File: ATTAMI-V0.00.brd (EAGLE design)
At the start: 22.8 x 22.9 mm, 26 parts, among them U1 MIC5225, U2 ATTINY85-20SU

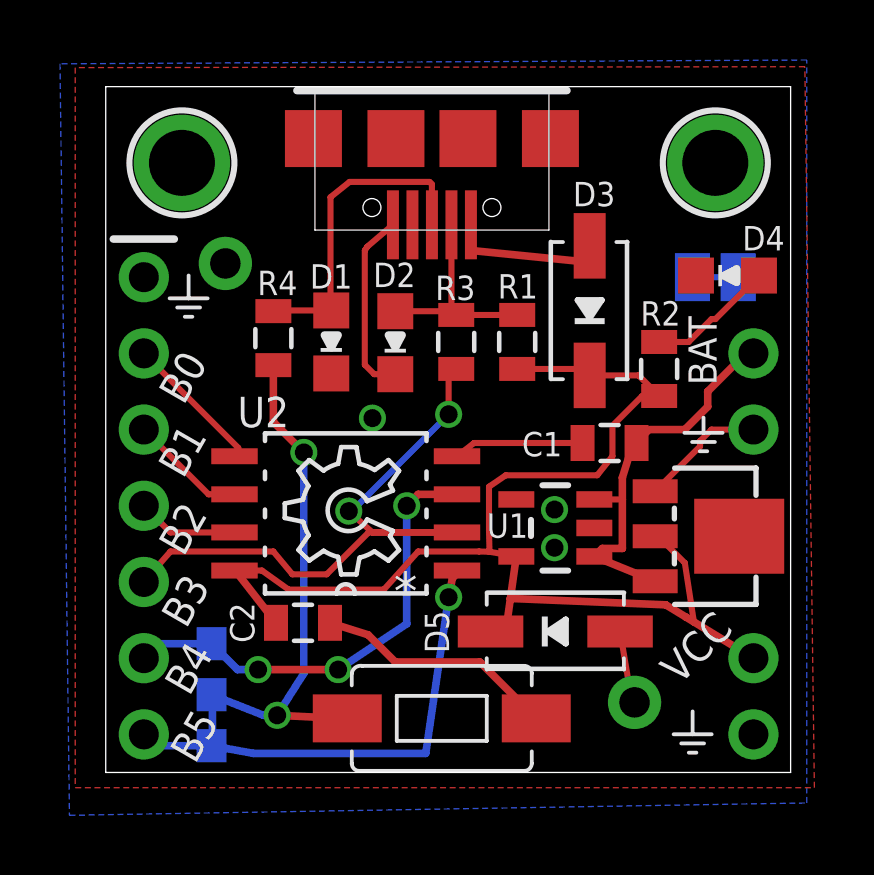
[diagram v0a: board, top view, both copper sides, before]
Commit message: pushed the pb5 wire a bit to the cneter
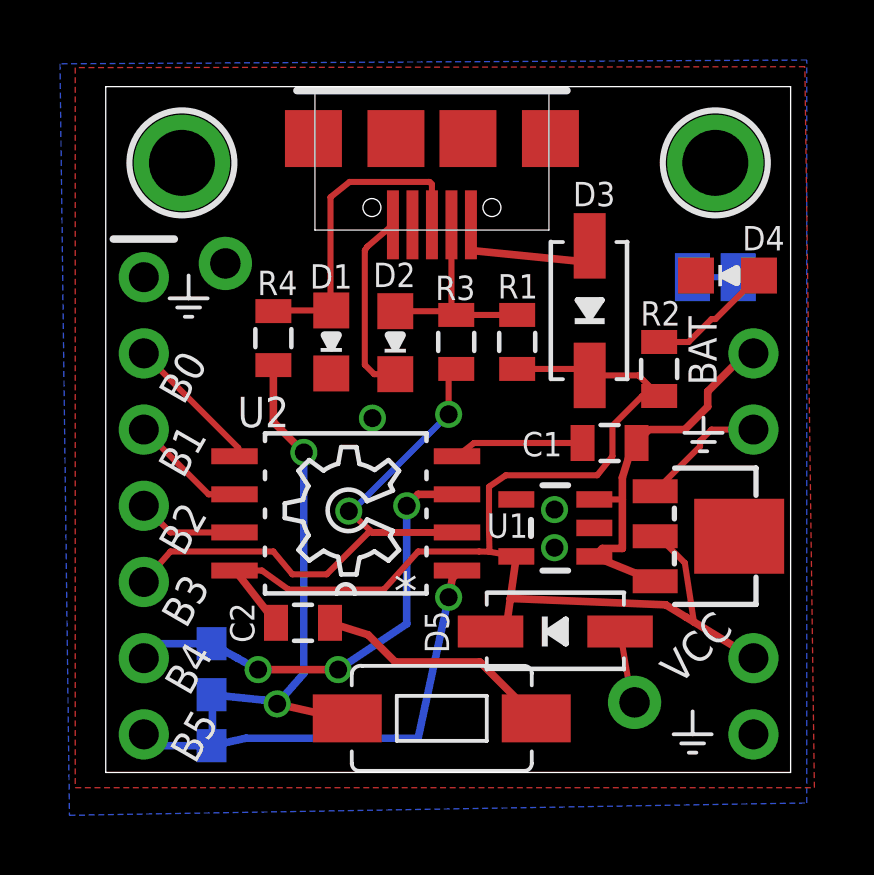
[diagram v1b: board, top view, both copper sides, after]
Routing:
- net PB5: track 15.8 -> 15.1 mm
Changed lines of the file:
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@@
 <wire x1="7.747" y1="3.429" x2="5.08" y2="3.429" width="0.254" layer="1"/>
 <via x="5.08" y="3.429" extent="1-16" drill="0.6"/>
-<wire x1="5.08" y1="3.429" x2="4.3924" y2="3.429" width="0.254" layer="16"/>
-<wire x1="4.3924" y1="3.429" x2="3.5306" y2="4.2908" width="0.254" layer="16"/>
+<wire x1="5.08" y1="3.429" x2="4.3924" y2="3.81" width="0.254" layer="16"/>
+<wire x1="4.3924" y1="3.81" x2="3.5306" y2="4.2908" width="0.254" layer="16"/>
 </signal>
 <signal name="PB5">
@@
 <wire x1="1.6492" y1="0.8908" x2="1.27" y2="1.27" width="0.254" layer="16"/>
 <via x="11.43" y="5.842" extent="1-16" drill="0.6"/>
-<wire x1="11.43" y1="5.842" x2="10.668" y2="0.635" width="0.254" layer="16"/>
-<wire x1="10.668" y1="0.635" x2="4.9294" y2="0.635" width="0.254" layer="16"/>
-<wire x1="4.9294" y1="0.635" x2="3.5306" y2="0.8908" width="0.254" layer="16"/>
+<wire x1="11.43" y1="5.842" x2="10.414" y2="1.143" width="0.254" layer="16"/>
+<wire x1="10.414" y1="1.143" x2="4.6754" y2="1.143" width="0.254" layer="16"/>
+<wire x1="4.6754" y1="1.143" x2="3.5306" y2="0.8908" width="0.254" layer="16"/>
 </signal>
 <signal name="V_BAT">
@@
 <contactref element="S1" pad="P$2"/>
 <wire x1="8.0514" y1="1.8034" x2="7.8486" y2="1.8034" width="0.254" layer="1"/>
-<wire x1="7.8486" y1="1.8034" x2="5.715" y2="1.905" width="0.254" layer="1"/>
-<via x="5.715" y="1.905" extent="1-16" drill="0.6"/>
-<wire x1="5.715" y1="1.905" x2="5.2578" y2="1.905" width="0.254" layer="16"/>
-<wire x1="5.2578" y1="1.905" x2="3.5306" y2="2.5908" width="0.254" layer="16"/>
+<wire x1="7.8486" y1="1.8034" x2="5.715" y2="2.286" width="0.254" layer="1"/>
+<via x="5.715" y="2.286" extent="1-16" drill="0.6"/>
+<wire x1="5.715" y1="2.286" x2="5.2578" y2="2.413" width="0.254" layer="16"/>
+<wire x1="5.2578" y1="2.413" x2="3.5306" y2="2.5908" width="0.254" layer="16"/>
 <wire x1="5.588" y1="13.578" x2="5.588" y2="11.684" width="0.254" layer="1"/>
 <wire x1="5.588" y1="11.684" x2="6.604" y2="10.668" width="0.254" layer="1"/>
 <via x="6.604" y="10.668" extent="1-16" drill="0.6"/>
 <wire x1="6.604" y1="10.668" x2="6.604" y2="3.302" width="0.254" layer="16"/>
-<wire x1="6.604" y1="3.302" x2="5.715" y2="1.905" width="0.254" layer="16"/>
+<wire x1="6.604" y1="3.302" x2="5.715" y2="2.286" width="0.254" layer="16"/>
 </signal>
 <signal name="N$3">

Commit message: hl version
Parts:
- SJ1: value (none) -> JUMPER-PAD-2-NC_BY_TRACE; device ATtami:SOLDERJUMPER_CLOSEDWIRE -> SparkFun-Passives:PAD-JUMPER-2-NC_BY_TRACE_YES_SILK
- SJ2: value (none) -> JUMPER-PAD-3-2OF3_NC_BY_TRACE_SMALL; device microbuilder:SOLDERJUMPER_2WAY_OPEN_0603 -> SparkFun-Passives:PAD-JUMPER-3-2OF3_NC_BY_TRACE_YES_SILK_FULL_BOX
- moved R2 0.28 mm to (18.7, 13.6)
- moved SJ1 0.23 mm to (20.5, 16.5)
- moved SJ2 0.22 mm to (3.45, 2.39)
- moved D3 0.18 mm to (16.3, 15.5)
- moved D4 0.18 mm to (20.6, 16.6), turned to 270 degrees
- moved D2 0.15 mm to (9.53, 14.2), turned to 0 degrees
- moved D1 0.05 mm to (7.47, 14.4), turned to 0 degrees
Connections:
- net GND: now also 1117.GND, S1.P$2, USB.GND; no longer 1117.1, S1.P$1, USB.GND@1
- net N$1: no longer S1.P$2
- net PB5: now also S1.P$1
- net VCC: now also 1117.VOUT@1, 1117.VOUT@2; no longer 1117.2
- net V_BAT: now also 1117.VIN; no longer 1117.3
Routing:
- net GND: track 23.3 -> 10.0 mm, vias 3 -> 2
- net VCC: track 42.2 -> 48.1 mm
- net PB5: track 15.1 -> 20.7 mm, vias 1 -> 2
- net N$7: track 11.6 -> 7.42 mm
- net N$13: track 0.00 -> 3.94 mm, vias 0 -> 1
- net PB4: track 15.4 -> 17.8 mm, vias 3 -> 2
- net N$1: track 16.6 -> 14.5 mm, vias 2 -> 1
- net N$3: track 1.40 -> 0.00 mm
- net PB3: track 22.0 -> 21.2 mm
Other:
- board text added: "4"
- board text added: "5"
- board text removed: "PB4"
- board text removed: "PB5"

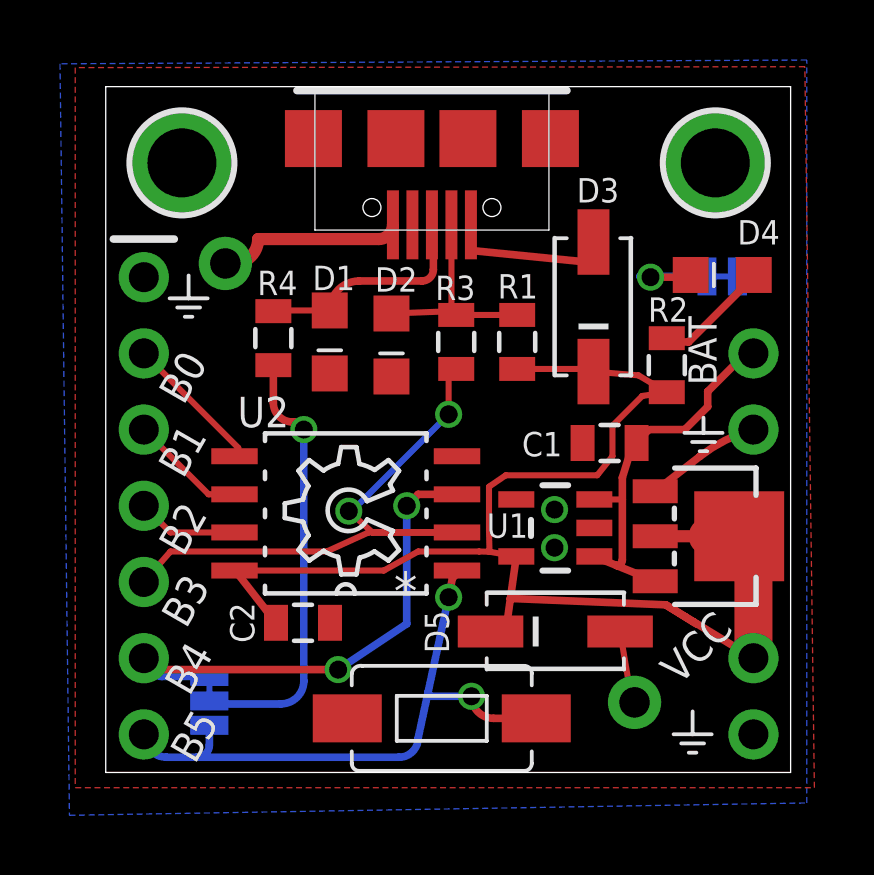
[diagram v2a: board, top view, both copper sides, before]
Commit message: Some changes of the routing
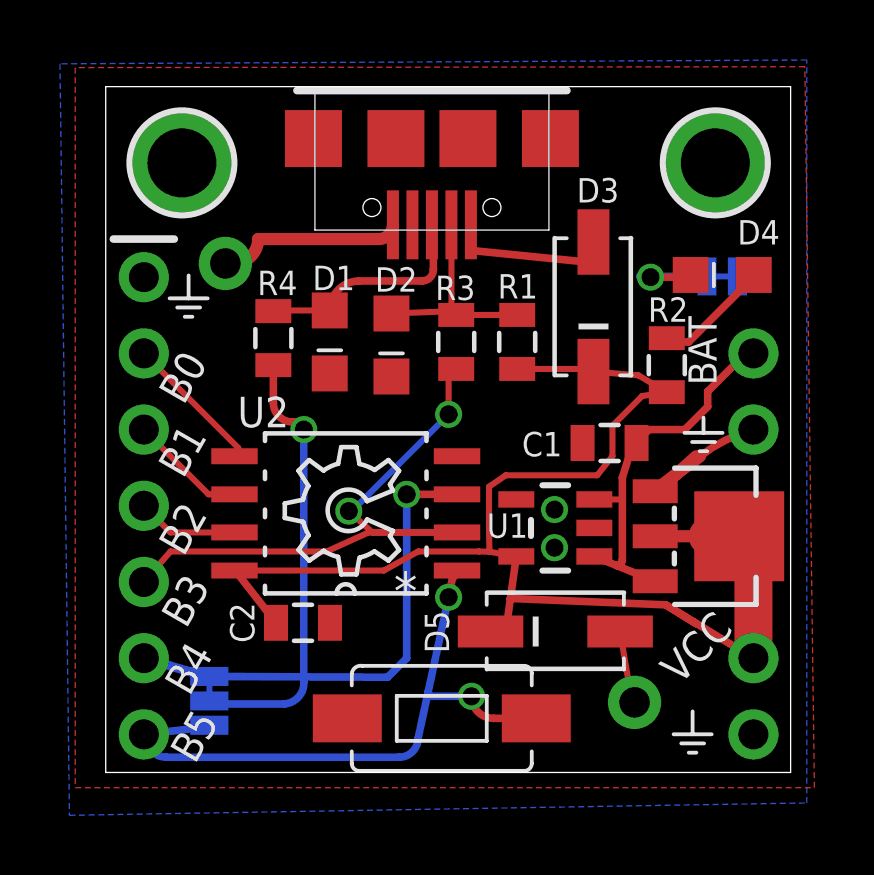
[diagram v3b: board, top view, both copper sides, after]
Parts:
- U3: value (none) -> 1117
- renumbered 1117 to U3
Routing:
- net GND: track 10.0 -> 12.0 mm
- net PB4: track 17.8 -> 16.2 mm, vias 2 -> 1
- net PB5: track 20.7 -> 21.6 mm
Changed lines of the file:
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@@
 <attribute name="NAME" x="4.3942" y="11.5062" size="1.016" layer="25" ratio="10" rot="SR0"/>
 </element>
-<element name="1117" library="ATtami" package="SOT89" value="" x="20.066" y="7.874" smashed="yes" rot="R270">
+<element name="U3" library="ATtami" package="SOT89" value="1117" x="20.066" y="7.874" smashed="yes" rot="R270">
 <attribute name="VALUE" x="16.241" y="10.079" size="1.27" layer="27" rot="R270"/>
 </element>
@@
 <contactref element="COIN_CELL_(-)" pad="1"/>
 <contactref element="U2" pad="4"/>
-<contactref element="1117" pad="GND"/>
 <via x="14.9606" y="8.763" extent="1-16" drill="0.6"/>
 <via x="14.9606" y="7.493" extent="1-16" drill="0.6"/>
@@
 <wire x1="5.08" y1="17.78" x2="4.2672" y2="16.9672" width="0.4064" layer="1" curve="-90"/>
 <wire x1="4.2672" y1="16.9672" x2="3.9878" y2="16.9672" width="0.4064" layer="1"/>
-<wire x1="18.316" y1="9.374" x2="19.812" y2="10.541" width="0.254" layer="1"/>
 <wire x1="19.812" y1="10.541" x2="21.59" y2="11.43" width="0.254" layer="1" curve="-22.784078"/>
+<contactref element="U3" pad="GND"/>
+<wire x1="18.288" y1="9.398" x2="19.812" y2="10.541" width="0.4064" layer="1"/>
+<wire x1="18.415" y1="9.398" x2="19.685" y2="10.541" width="0.4064" layer="1"/>
+<wire x1="18.288" y1="9.398" x2="18.415" y2="9.398" width="0.4064" layer="1"/>
+<wire x1="18.542" y1="9.398" x2="18.415" y2="9.398" width="0.4064" layer="1"/>
+<wire x1="18.288" y1="9.398" x2="18.316" y2="9.374" width="0" layer="19" extent="1-1"/>
 </signal>
 <signal name="PB3">
@@
 <contactref element="J1" pad="6"/>
 <contactref element="U2" pad="3"/>
-<wire x1="11.7094" y1="9.271" x2="10.414" y2="9.271" width="0.254" layer="1"/>
-<wire x1="10.414" y1="9.271" x2="10.033" y2="8.89" width="0.254" layer="1"/>
-<via x="10.033" y="8.89" extent="1-16" drill="0.6"/>
-<wire x1="10.033" y1="8.89" x2="10.033" y2="4.953" width="0.254" layer="16"/>
-<wire x1="10.033" y1="4.953" x2="7.747" y2="3.429" width="0.254" layer="16"/>
-<via x="7.747" y="3.429" extent="1-16" drill="0.6"/>
 <contactref element="SJ2" pad="3"/>
-<wire x1="3.4544" y1="3.2004" x2="1.8796" y2="3.2004" width="0.254" layer="16"/>
-<wire x1="1.8796" y1="3.2004" x2="1.27" y2="3.81" width="0.254" layer="16" curve="-90"/>
-<wire x1="7.747" y1="3.429" x2="1.27" y2="3.429" width="0.254" layer="1"/>
-<wire x1="1.27" y1="3.429" x2="1.27" y2="3.81" width="0.254" layer="1"/>
+<wire x1="3.429" y1="3.175" x2="1.27" y2="3.81" width="0.3048" layer="16"/>
+<wire x1="3.4544" y1="3.2004" x2="9.398" y2="3.175" width="0.254" layer="16"/>
+<wire x1="9.398" y1="3.175" x2="10.033" y2="3.81" width="0.254" layer="16"/>
+<wire x1="10.033" y1="3.81" x2="10.033" y2="9.271" width="0.254" layer="16"/>
+<via x="10.033" y="9.271" extent="1-16" drill="0.6"/>
+<wire x1="10.033" y1="9.271" x2="11.7094" y2="9.271" width="0.254" layer="1"/>
+<wire x1="3.429" y1="3.175" x2="3.4544" y2="3.2004" width="0" layer="19" extent="16-16"/>
 </signal>
 <signal name="PB5">
@@
 <wire x1="10.74226875" y1="2.661240625" x2="10.414" y2="1.143" width="0.254" layer="16"/>
 <wire x1="10.414" y1="1.143" x2="9.779" y2="0.508" width="0.254" layer="16" curve="-90"/>
-<wire x1="9.779" y1="0.508" x2="3.048" y2="0.508" width="0.254" layer="16"/>
-<wire x1="3.048" y1="0.508" x2="2.032" y2="0.508" width="0.254" layer="16"/>
+<wire x1="9.779" y1="0.508" x2="2.032" y2="0.508" width="0.254" layer="16"/>
 <wire x1="2.032" y1="0.508" x2="1.27" y2="1.27" width="0.254" layer="16" curve="-90"/>
-<contactref element="SJ2" pad="1"/>
 <contactref element="S1" pad="P$1"/>
-<wire x1="3.4544" y1="1.5748" x2="3.4544" y2="0.9144" width="0.254" layer="16"/>
-<wire x1="3.4544" y1="0.9144" x2="3.048" y2="0.508" width="0.254" layer="16" curve="-90"/>
 <wire x1="14.3514" y1="1.8034" x2="12.9286" y2="1.8034" width="0.254" layer="1"/>
 <wire x1="12.9286" y1="1.8034" x2="12.192" y2="2.54" width="0.254" layer="1" curve="-90"/>
@@
 <wire x1="12.192" y1="2.54" x2="10.863509375" y2="2.54" width="0.254" layer="16"/>
 <wire x1="10.863509375" y1="2.54" x2="10.74226875" y2="2.661240625" width="0.254" layer="16" curve="-90"/>
+<contactref element="SJ2" pad="1"/>
+<wire x1="3.429" y1="1.524" x2="1.27" y2="1.27" width="0.254" layer="16"/>
+<wire x1="3.429" y1="1.524" x2="3.4544" y2="1.5748" width="0" layer="19" extent="16-16"/>
 </signal>
 <signal name="V_BAT">
-<contactref element="1117" pad="VIN"/>
+<contactref element="U3" pad="VIN"/>
 <contactref element="J2" pad="1"/>
 <contactref element="U1" pad="1"/>
@@
 <contactref element="J3" pad="1"/>
 <contactref element="U2" pad="8"/>
-<contactref element="1117" pad="VOUT@1"/>
+<contactref element="U3" pad="VOUT@1"/>
 <wire x1="18.316" y1="7.874" x2="18.415" y2="7.874" width="0.2032" layer="1"/>
 <wire x1="13.716" y1="13.451" x2="15.916478125" y2="13.451" width="0.2032" layer="1"/>
@@
 <wire x1="19.337809375" y1="5.1809" x2="18.669" y2="5.588" width="0.254" layer="1"/>
 <wire x1="18.669" y1="5.588" x2="13.489453125" y2="5.8002125" width="0.254" layer="1"/>
-<contactref element="1117" pad="VOUT@2"/>
+<contactref element="U3" pad="VOUT@2"/>
 <wire x1="18.415" y1="7.874" x2="20.066" y2="7.874" width="0.4064" layer="1"/>
 <wire x1="20.066" y1="7.874" x2="21.116" y2="7.874" width="0.4064" layer="1"/>
@@
 <via x="6.604" y="11.43" extent="1-16" drill="0.6" diameter="0.254"/>
 <wire x1="6.604" y1="11.43" x2="6.604" y2="3.048" width="0.254" layer="16"/>
-<wire x1="6.604" y1="3.048" x2="5.842" y2="2.286" width="0.254" layer="16" curve="-90"/>
-<wire x1="5.842" y1="2.286" x2="3.556" y2="2.286" width="0.254" layer="16"/>
+<wire x1="6.604" y1="3.048" x2="5.969" y2="2.286" width="0.254" layer="16" curve="-90"/>
+<wire x1="5.969" y1="2.286" x2="3.556" y2="2.286" width="0.254" layer="16"/>
 <wire x1="3.556" y1="2.286" x2="3.4544" y2="2.3876" width="0.254" layer="16" curve="-90"/>
 </signal>
